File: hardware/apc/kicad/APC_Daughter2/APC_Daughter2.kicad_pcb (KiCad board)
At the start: 2 copper layers, 42.4 x 29.2 mm, 16 parts, among them IC1 AD8319ACPZ-R7, J1 Conn_Coaxial, J2 Conn_Coaxial, J3 Conn_01x05, J4 Conn_01x05, U1 EP2W1_, U2 tfa32

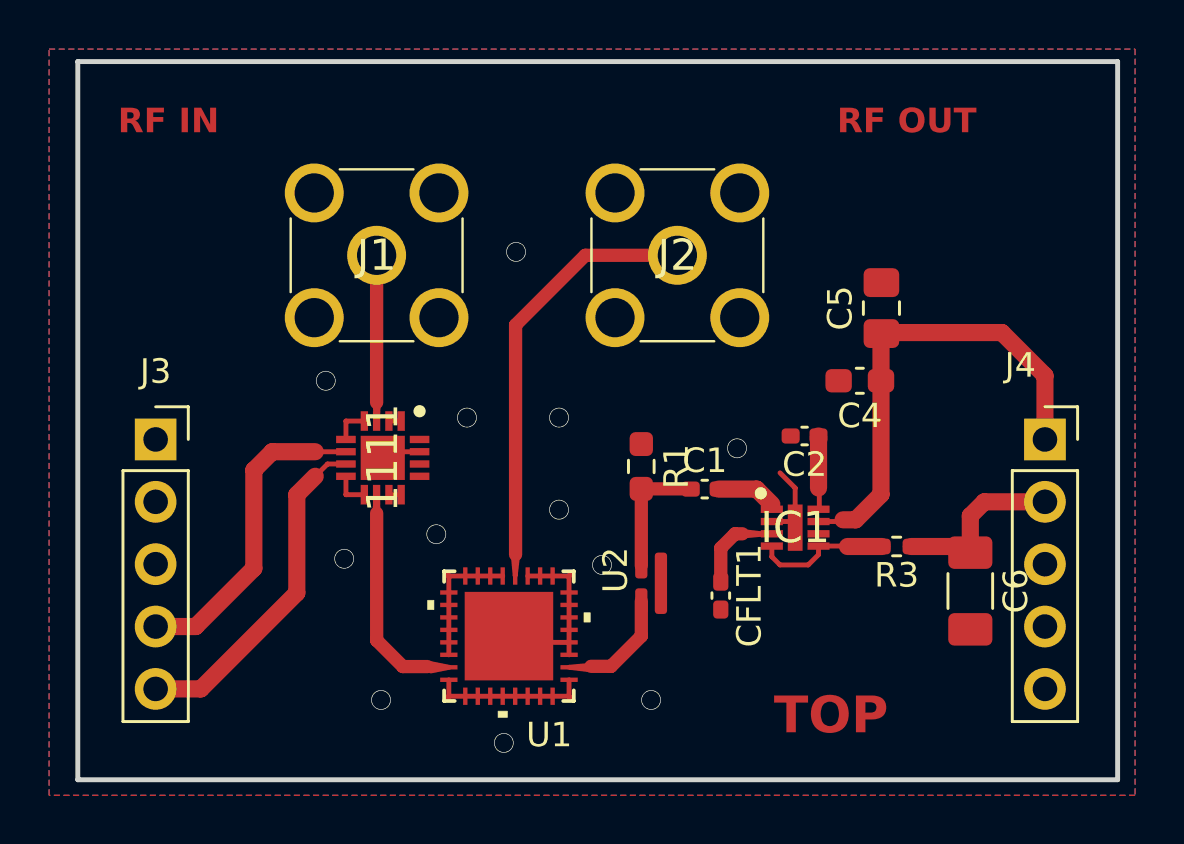
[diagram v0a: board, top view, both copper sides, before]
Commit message: Update APC and LO
1) Add 30dB of fixed attenuation in feedback line of APC for better
   linearity of the power meter
2) Add power splitter for single ended outputs of the local oscillator
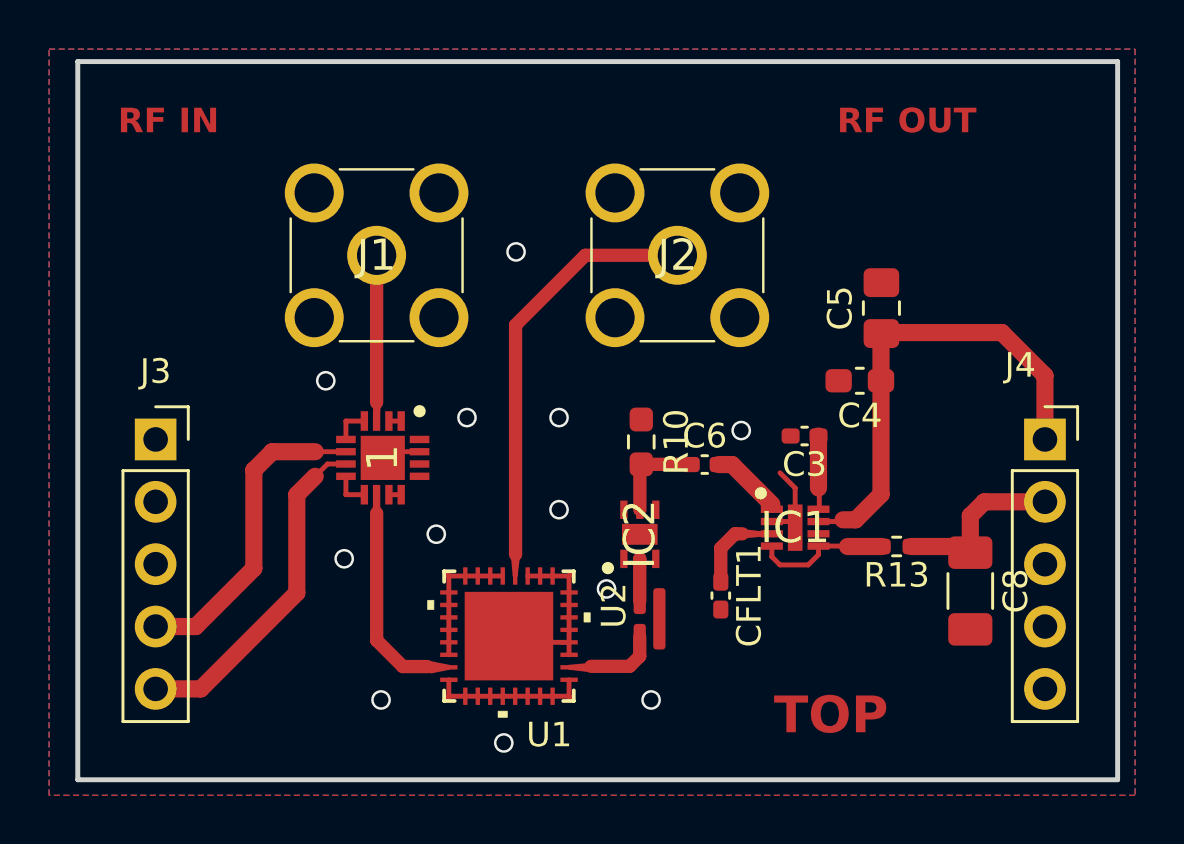
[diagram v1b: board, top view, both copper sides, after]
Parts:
- added IC2: HMC658LP2E, footprints:SON65P200X200X105-7N, F.Cu at (140.0, 101.3)
- U2: value tfa32 -> TFA32C10DB
- moved U2 1.45 mm to (140.8, 104.7)
- moved C6 1.00 mm to (142.7, 98.4)
- moved R10 1.00 mm to (140.1, 97.5)
- renumbered 1111 to 1, C2 to C3, C1 to C6, C6 to C8, R1 to R10, R3 to R13
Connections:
- U2 pad 2: /SIGNAL -> Net-(IC2-RF1)
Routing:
- net Net-(IC2-RF1): track 0.00 -> 1.72 mm
- net /SIGNAL: track 5.13 -> 3.90 mm
- net /PORT2: track 3.98 -> 2.95 mm
